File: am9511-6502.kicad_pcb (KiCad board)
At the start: 2 copper layers, 84.9 x 67.5 mm, 24 parts, among them J1 Conn_01x18_Pin, U1 AM9511A, U2 GAL16V8, U3 74HC112, U4 ADA-TPS61040, U5 74HC123, X1 4 MHz

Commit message: additional PCB cleanup
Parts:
- D1, D2: footprint LED_THT:LED_D5.0mm -> LED_THT:LED_D3.0mm
- J1: footprint Connector_PinHeader_2.54mm:PinHeader_1x18_P2.54mm_Horizontal -> am9511-6502-footprints:PinHeader_1x18_P2.54mm_Horizontal
- U2: value GAL16V8 -> ATF16V8B
- moved J1 4.19 mm to (179.2, 62.5)
- moved C1 3.40 mm to (127.4, 90.7)
- moved C2 3.40 mm to (140.2, 59.0)
- moved C3 3.40 mm to (122.4, 58.7)
- moved C4 3.40 mm to (122.2, 90.7)
- moved C5 3.40 mm to (130.9, 98.7)
- moved C6 3.40 mm to (150.2, 69.5)
- moved D3 3.40 mm to (115.7, 83.4)
- moved R2 3.40 mm to (134.6, 90.7)
- moved U1 3.40 mm to (153.4, 67.0)
- moved U2 3.40 mm to (133.6, 62.1)
- moved U3 3.40 mm to (115.8, 62.1)
- moved U4 3.40 mm to (157.5, 107.0)
- moved U5 3.40 mm to (115.8, 94.1)
- moved X1 3.40 mm to (132.5, 110.8)
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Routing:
- net Net-(U1-CLK): track 59.6 -> 54.9 mm
- net VCC: track 278.6 -> 281.8 mm
- net Net-(D2-K): track 21.7 -> 19.5 mm
- net /~{IRQ}: track 42.4 -> 43.2 mm
- net /~{CS}: track 74.5 -> 75.3 mm
- net /D7: track 11.6 -> 12.4 mm
- net /D6: track 17.2 -> 18.0 mm
- net /D5: track 22.2 -> 23.0 mm
- net /RESET: track 49.7 -> 49.0 mm
- net /PHI2: track 92.9 -> 92.3 mm
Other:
- board size 84.9 x 67.5 mm -> 82.1 x 67.5 mm
- board text added: "~{RES}"
- board text removed: "ceharris414@gmail.com"
- board text removed: "~{RESET}"

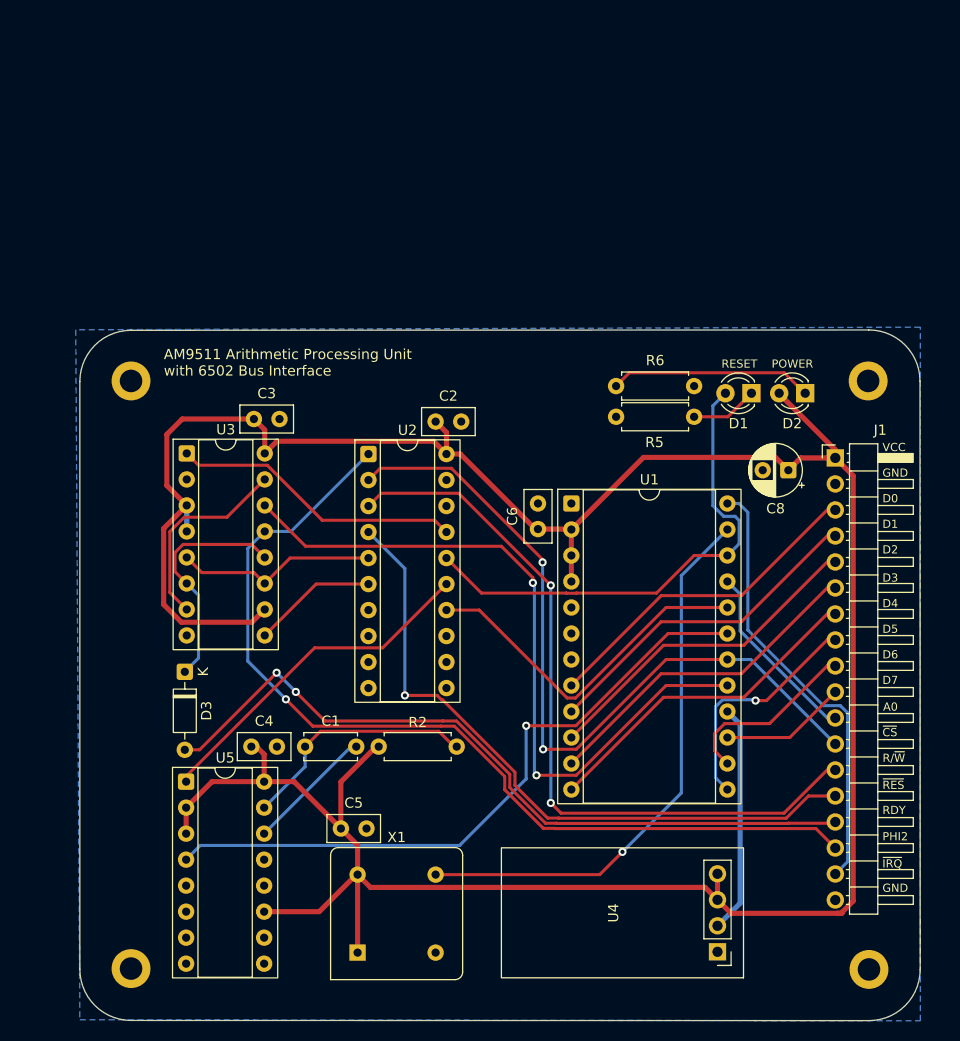
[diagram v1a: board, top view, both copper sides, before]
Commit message: reset schematic annotations
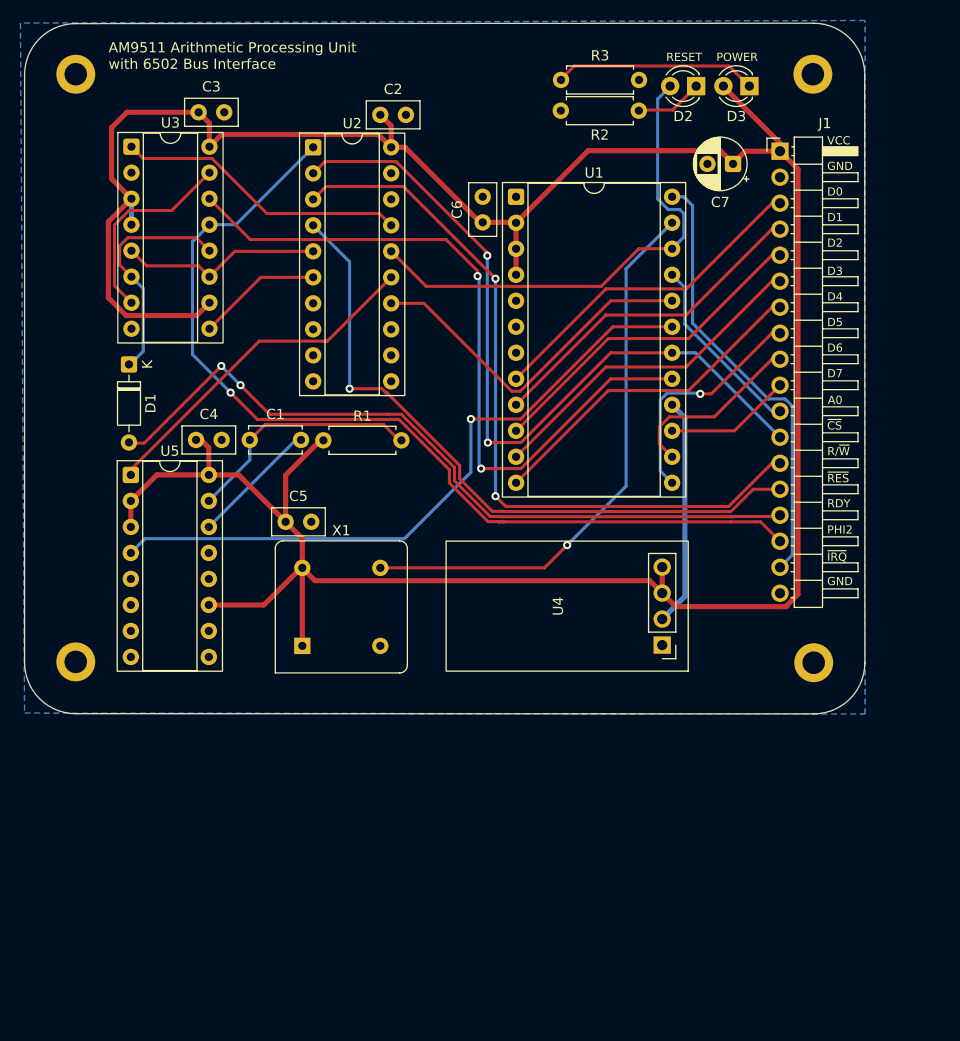
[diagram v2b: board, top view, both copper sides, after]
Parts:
- removed C8: 1µF, Capacitor_THT:CP_Radial_D5.0mm_P2.50mm
- removed R5: 470, Resistor_THT:R_Axial_DIN0207_L6.3mm_D2.5mm_P7.62mm_Horizontal
- removed R6: 1K, Resistor_THT:R_Axial_DIN0207_L6.3mm_D2.5mm_P7.62mm_Horizontal
- added C7: 1µF, Capacitor_THT:CP_Radial_D5.0mm_P2.50mm, F.Cu at (169.2, 33.8)
- added R1: 2K4, Resistor_THT:R_Axial_DIN0207_L6.3mm_D2.5mm_P7.62mm_Horizontal, F.Cu at (129.2, 60.8)
- added R3: 1K, Resistor_THT:R_Axial_DIN0207_L6.3mm_D2.5mm_P7.62mm_Horizontal, F.Cu at (152.4, 25.6)
- D1: value YELLOW -> 1N914; footprint LED_THT:LED_D3.0mm -> Diode_THT:D_DO-35_SOD27_P7.62mm_Horizontal
- D2: value BLUE -> YELLOW
- D3: value 1N914 -> BLUE; footprint Diode_THT:D_DO-35_SOD27_P7.62mm_Horizontal -> LED_THT:LED_D3.0mm
- R2: value 2K4 -> 470
- moved D3 79.5 mm to (170.8, 26.2), turned to 180 degrees
- moved R2 67.1 mm to (160.0, 28.6), turned to 180 degrees
- moved D1 60.9 mm to (110.2, 53.4), turned to -90 degrees
- moved D2 31.8 mm to (165.6, 26.2)
- moved H3 30.4 mm to (105.0, 82.4)
- moved X1 30.4 mm to (127.1, 80.9)
- moved C1 30.4 mm to (122.0, 60.8)
- moved C4 30.4 mm to (116.8, 60.8)
- moved C6 30.4 mm to (144.8, 39.5)
- moved H1 30.4 mm to (105.0, 25.0)
- moved H2 30.4 mm to (177.0, 25.0)
- moved U1 30.4 mm to (148.0, 37.0)
- moved U2 30.4 mm to (128.2, 32.2)
- moved U3 30.4 mm to (110.4, 32.1)
- moved C2 30.4 mm to (134.8, 29.0)
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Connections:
- D1 pad 2: /RESET -> /RDY
- D2 pad 2: VCC -> /RESET
- D3 pad 2: /RDY -> VCC
- R2 pad 1: VCC -> Net-(D2-K)
- R2 pad 2: Net-(U5A-RCext) -> GND
- U3 pad 12: Net-(D3-K) -> Net-(D1-K)
- U3 pad 6: Net-(D3-K) -> Net-(D1-K)
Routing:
- net Net-(D1-K): track 6.55 -> 22.8 mm
- net Net-(D2-K): track 19.5 -> 6.55 mm
- net Net-(D3-K): track 22.8 -> 19.5 mm
